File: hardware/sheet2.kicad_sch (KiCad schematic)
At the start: 0 parts

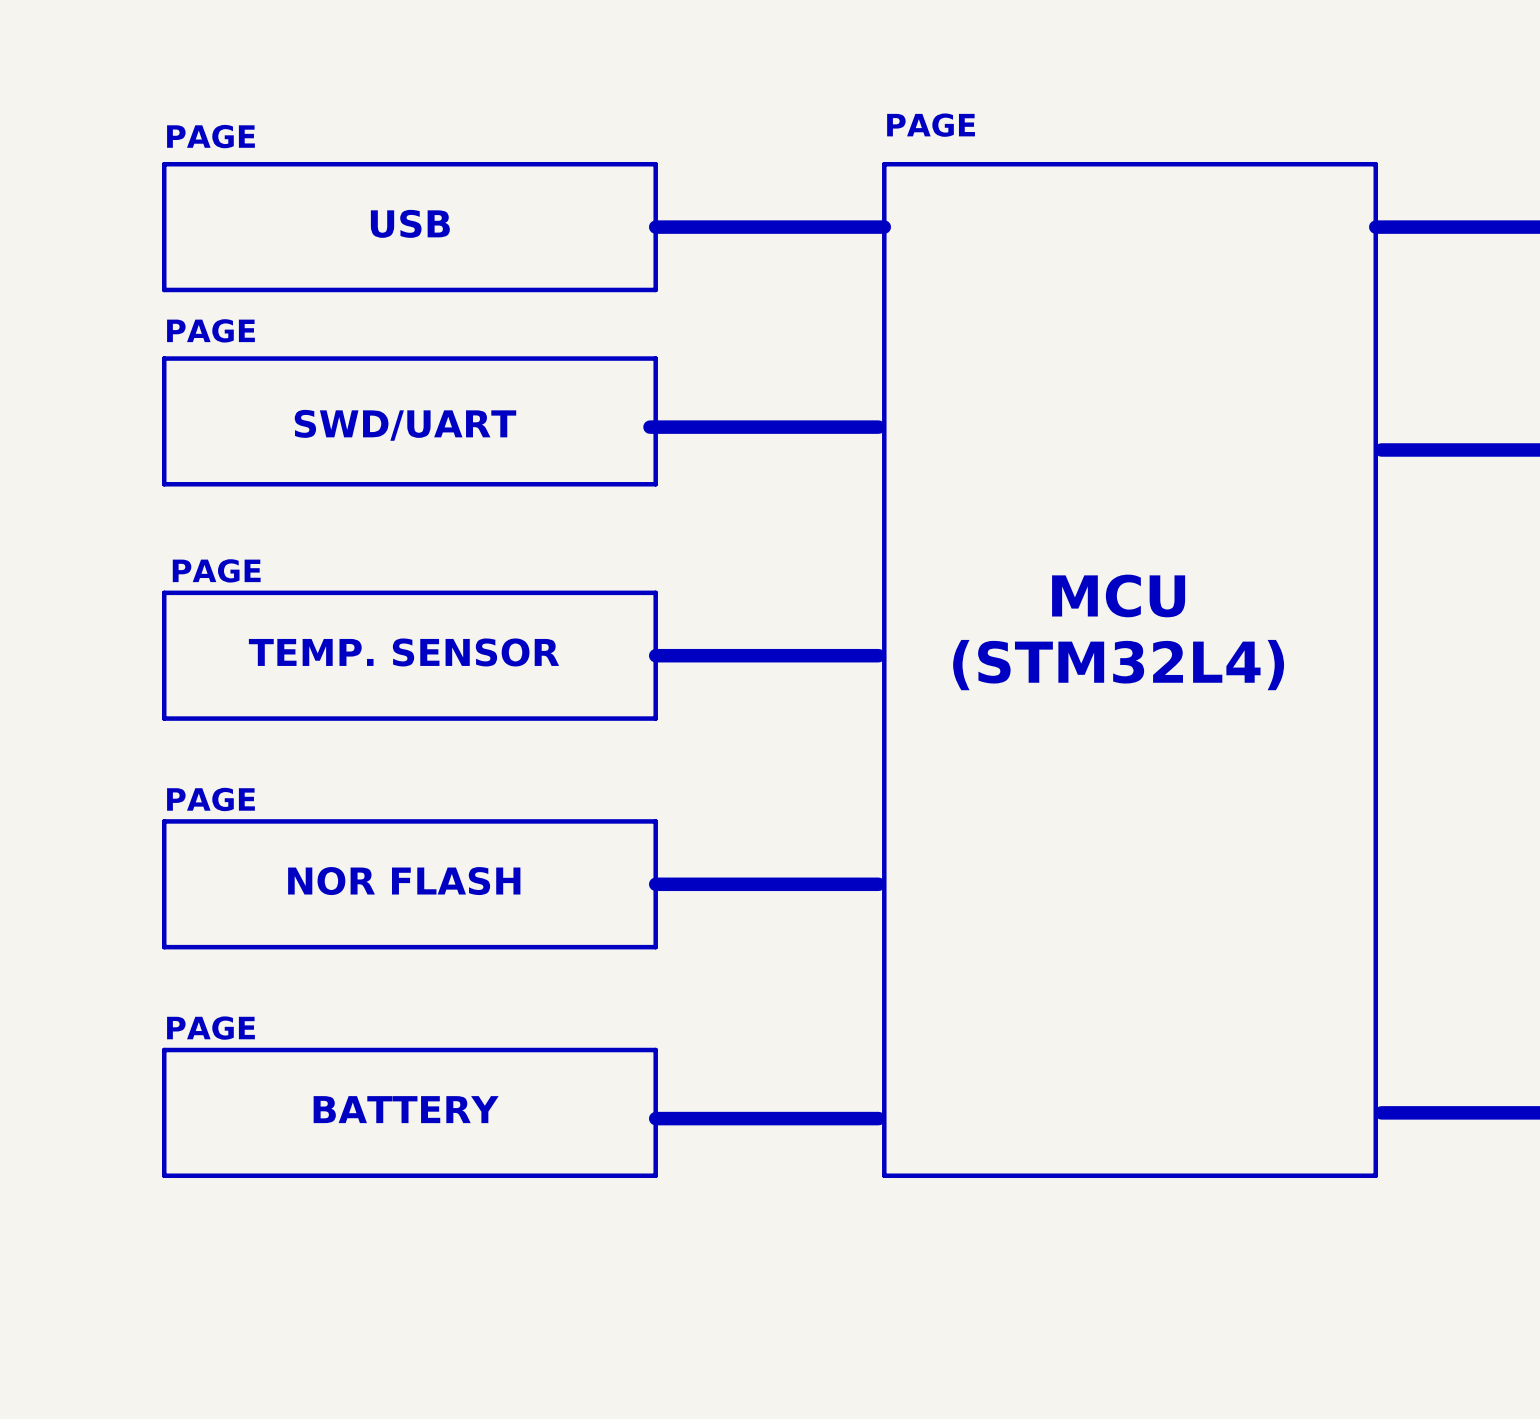
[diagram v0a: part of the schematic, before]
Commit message: hardware(feat): add 4xButton
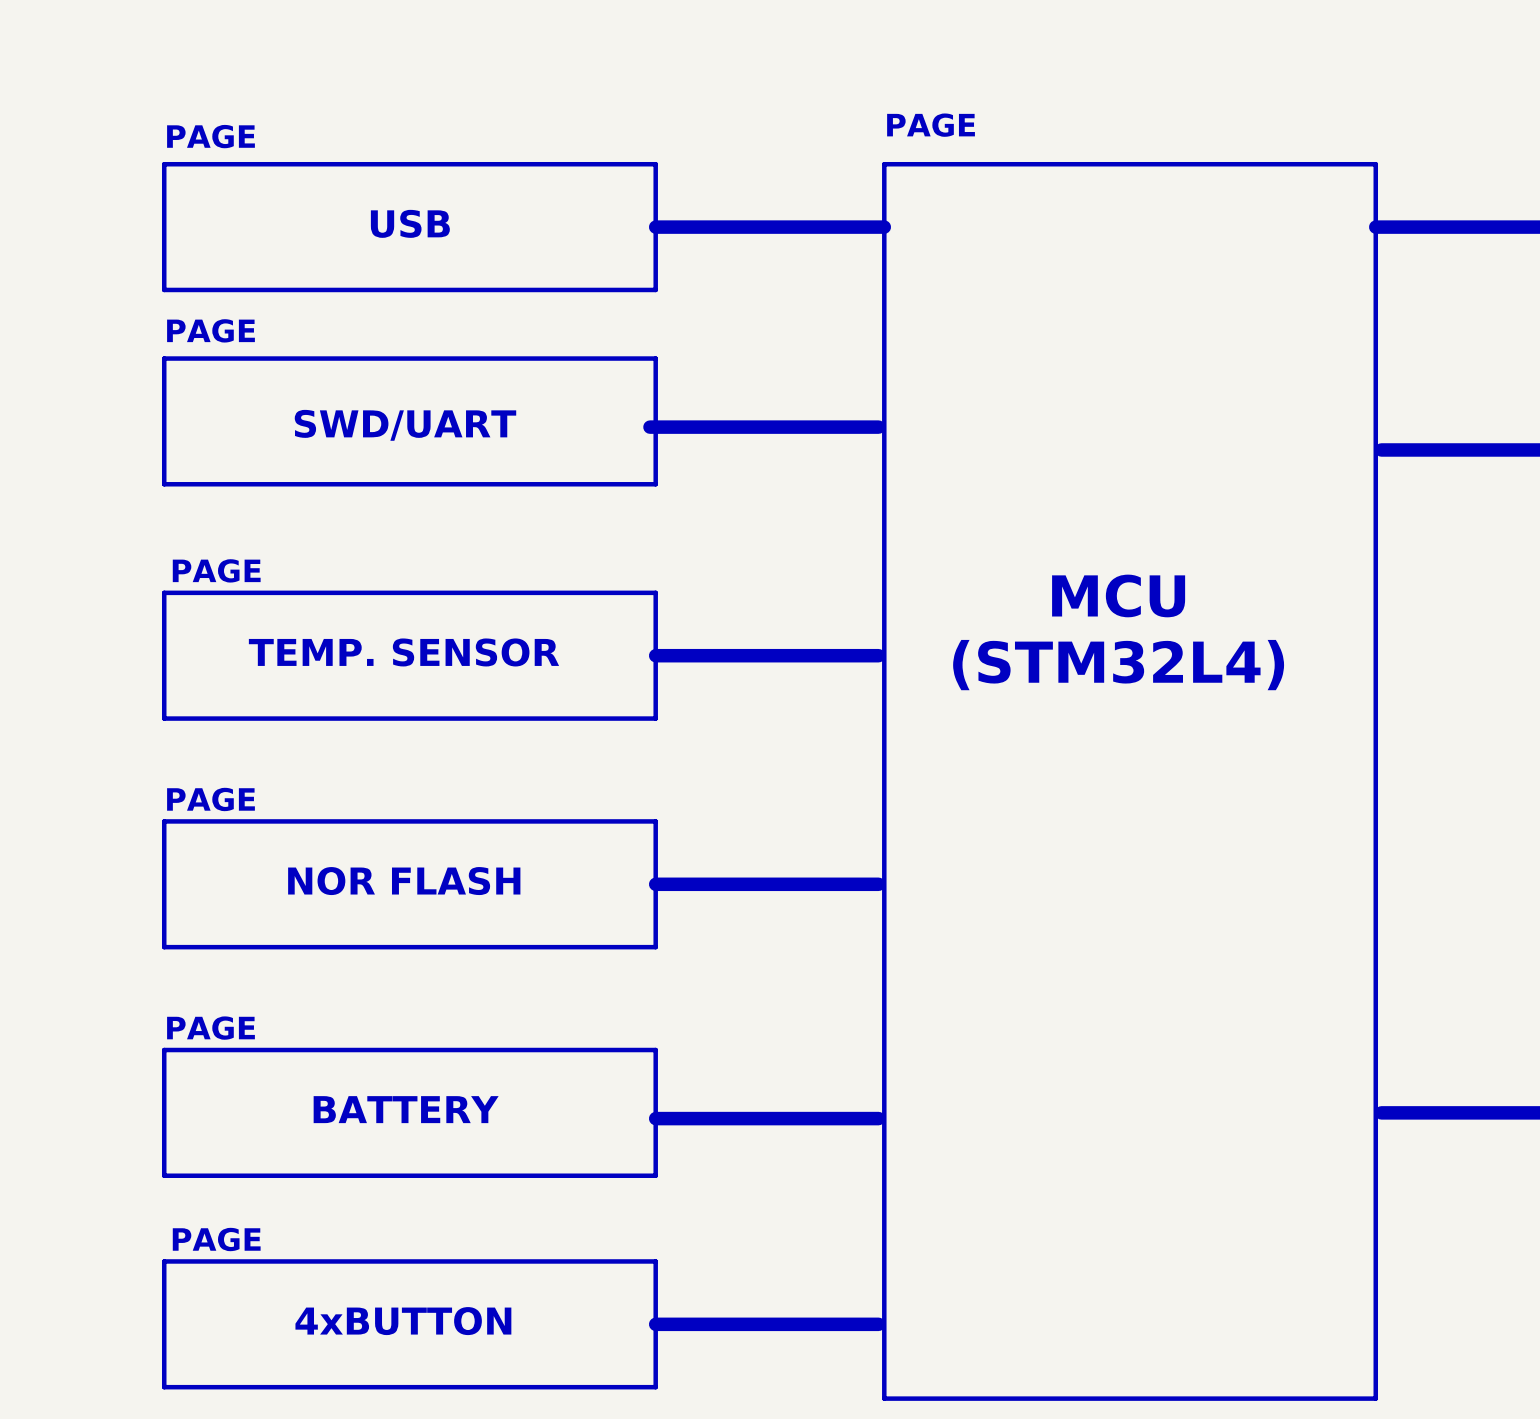
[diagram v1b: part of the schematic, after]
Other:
- note added: "4xBUTTON"
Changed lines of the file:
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@@
+	)
+	(rectangle
+		(start 76.2 248.92)
+		(end 130.81 262.89)
+		(stroke
+			(width 0.5)
+			(type solid)
+			(color 0 0 0 1)
+		)
+		(fill
+			(type color)
+			(color 194 194 194 1)
+		)
 	)
 	(rectangle
@@
 	(rectangle
 		(start 156.21 127)
-		(end 210.82 239.395)
+		(end 210.82 264.16)
 		(stroke
 			(width 0.5)
@@
 	(text "PAGE"
 		(exclude_from_sim no)
+		(at 76.835 248.285 0)
+		(effects
+			(font
+				(face "Arial")
+				(size 2.5 2.5)
+				(bold yes)
+				(color 0 0 0 1)
+			)
+			(justify left bottom)
+		)
+	)
+	(text "PAGE"
+		(exclude_from_sim no)
 		(at 237.49 224.79 0)
 		(effects
@@
 		)
 	)
+	(text "4xBUTTON"
+		(exclude_from_sim no)
+		(at 102.87 255.905 0)
+		(effects
+			(font
+				(face "Arial")
+				(size 3 3)
+				(bold yes)
+				(color 0 0 0 1)
+			)
+		)
+	)
 	(text "PAGE"
 		(exclude_from_sim no)
@@
 		)
 	)
+	(polyline
+		(pts
+			(xy 130.81 255.905) (xy 155.575 255.905)
+		)
+		(stroke
+			(width 1.5)
+			(type solid)
+			(color 0 0 255 1)
+		)
+	)

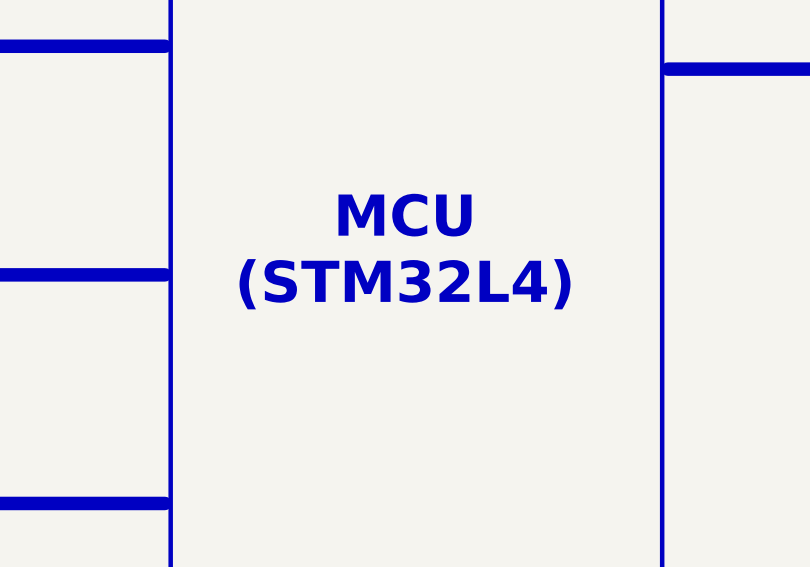
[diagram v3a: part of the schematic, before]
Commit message: hardware(feat): add led indications
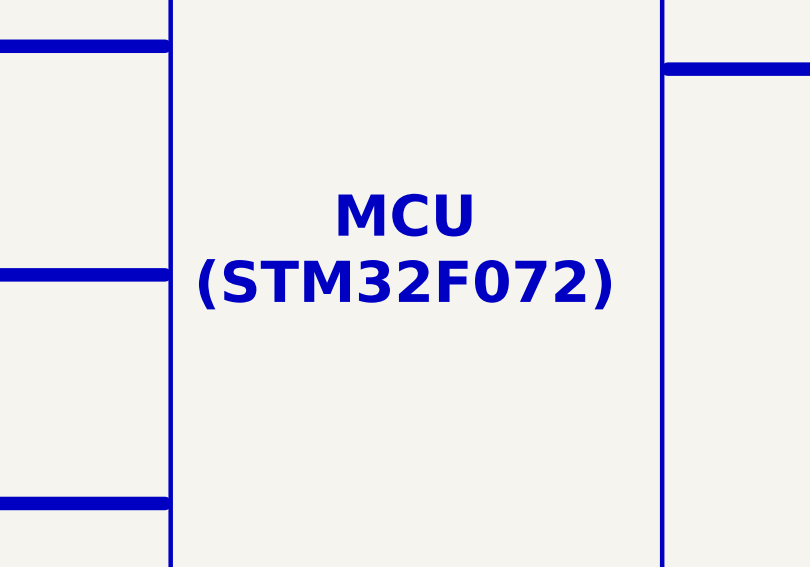
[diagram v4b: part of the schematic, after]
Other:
- note added: "MCU (STM32F072)"
- note removed: "MCU (STM32L4)"
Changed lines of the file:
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@@
 		(rev "A")
 		(company "Sleman")
-		(comment 1 "For more designs, visit")
-		(comment 2 "www.github.com/slemanz")
+		(comment 1 "For more designs, visit www.github.com/slemanz")
 	)
 	(rectangle
@@
 		)
 	)
-	(text "MCU\n(STM32L4)"
+	(text "MCU\n(STM32F072)"
 		(exclude_from_sim no)
 		(at 182.245 179.07 0)

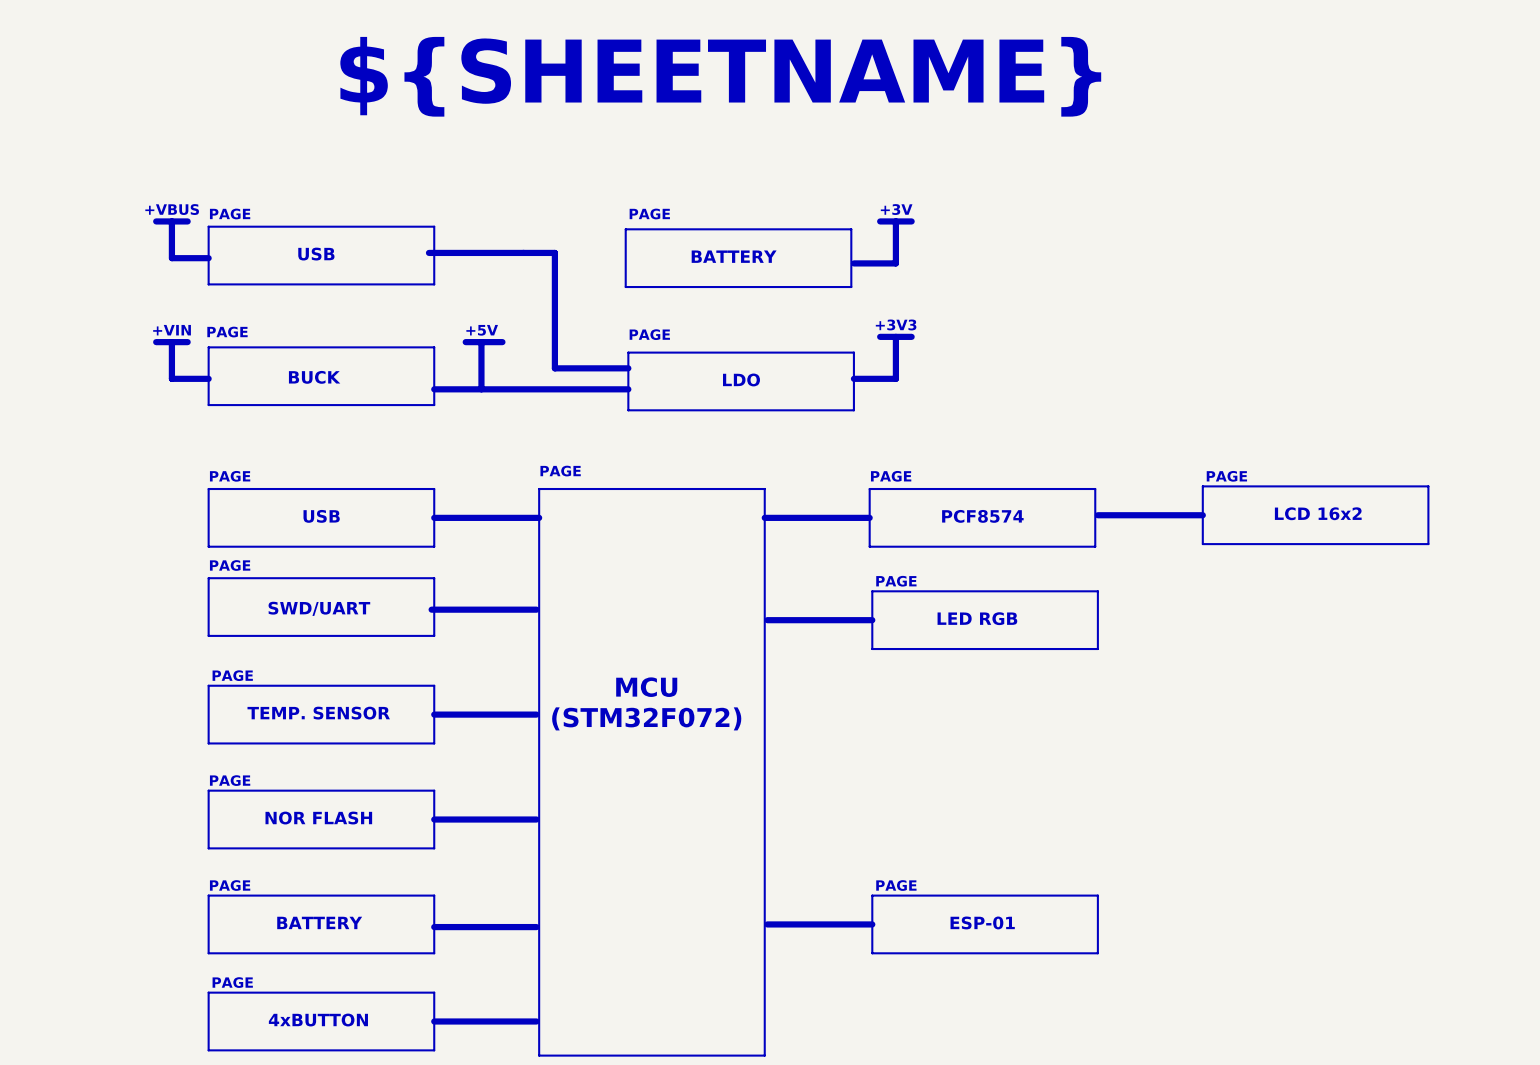
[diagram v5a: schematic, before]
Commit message: hardware(feat): update block diagram with page references
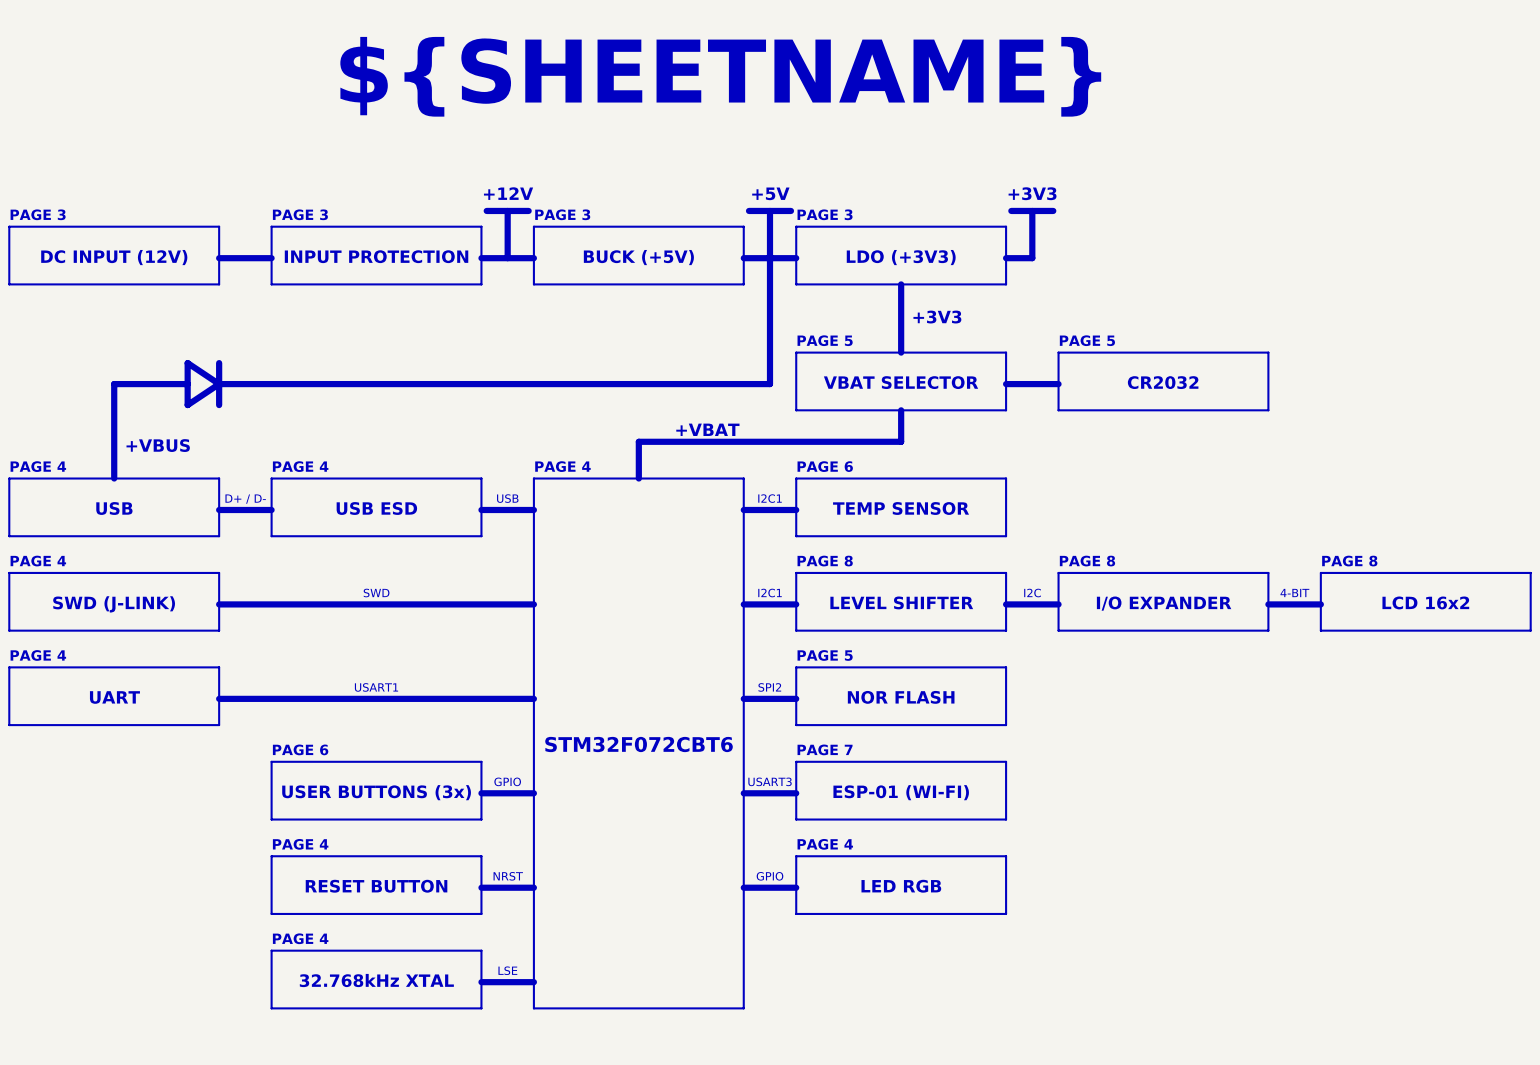
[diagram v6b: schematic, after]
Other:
- note added: "+12V"
- note added: "+VBAT"
- note added: "32.768kHz XTAL"
- note added: "4-BIT"
- note added: "BUCK (+5V)"
- note added: "CR2032"
- note added: "D+ / D-"
- note added: "DC INPUT (12V)"
- note added: "ESP-01 (WI-FI)"
- note added: "GPIO"
- note added: "I/O EXPANDER"
- note added: "I2C"
- note added: "I2C1"
- note added: "INPUT PROTECTION"
- note added: "LDO (+3V3)"
- note added: "LEVEL SHIFTER"
- note added: "LSE"
- note added: "NRST"
- note added: "PAGE 3"
- note added: "PAGE 4"
- note added: "PAGE 5"
- note added: "PAGE 6"
- note added: "PAGE 7"
- note added: "PAGE 8"
- note added: "RESET BUTTON"
- note added: "SPI2"
- note added: "STM32F072CBT6"
- note added: "SWD"
- note added: "SWD (J-LINK)"
- note added: "TEMP SENSOR"
- note added: "UART"
- note added: "USART1"
- note added: "USART3"
- note added: "USB ESD"
- note added: "USER BUTTONS (3x)"
- note added: "VBAT SELECTOR"
- note removed: "+3V"
- note removed: "+VIN"
- note removed: "4xBUTTON"
- note removed: "BATTERY"
- note removed: "BUCK"
- note removed: "ESP-01"
- note removed: "LDO"
- note removed: "MCU (STM32F072)"
- note removed: "PAGE"
- note removed: "PCF8574"
- note removed: "SWD/UART"
- note removed: "TEMP. SENSOR"
